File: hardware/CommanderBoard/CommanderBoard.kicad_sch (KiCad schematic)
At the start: 42 parts, among them J1 Conn_01x22, J1BUS1 Conn_02x04_Odd_Even, J1BUS2 Conn_02x04_Odd_Even, J2 Conn_01x22, J2BUS1 Conn_01x02, J2BUS2 Conn_01x02, J3 HUB75, J4 Conn_01x22, SW1 SW_SPDT, SW2 SW_DP3T, SW3 SW_DP3T, SW4 SW_DP3T

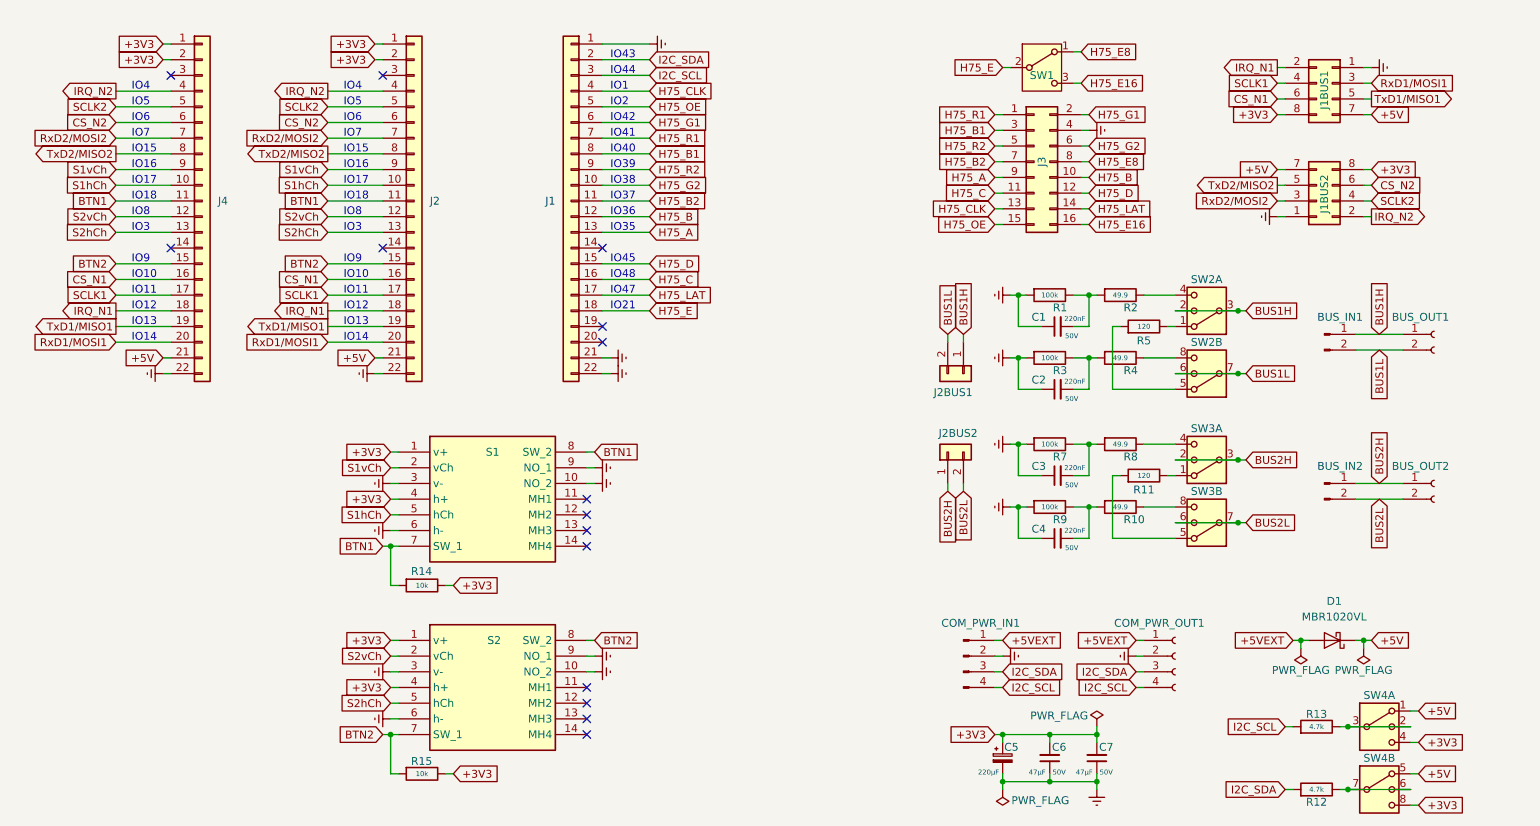
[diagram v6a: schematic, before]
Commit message: Minor imrpovements in positions and footprints.
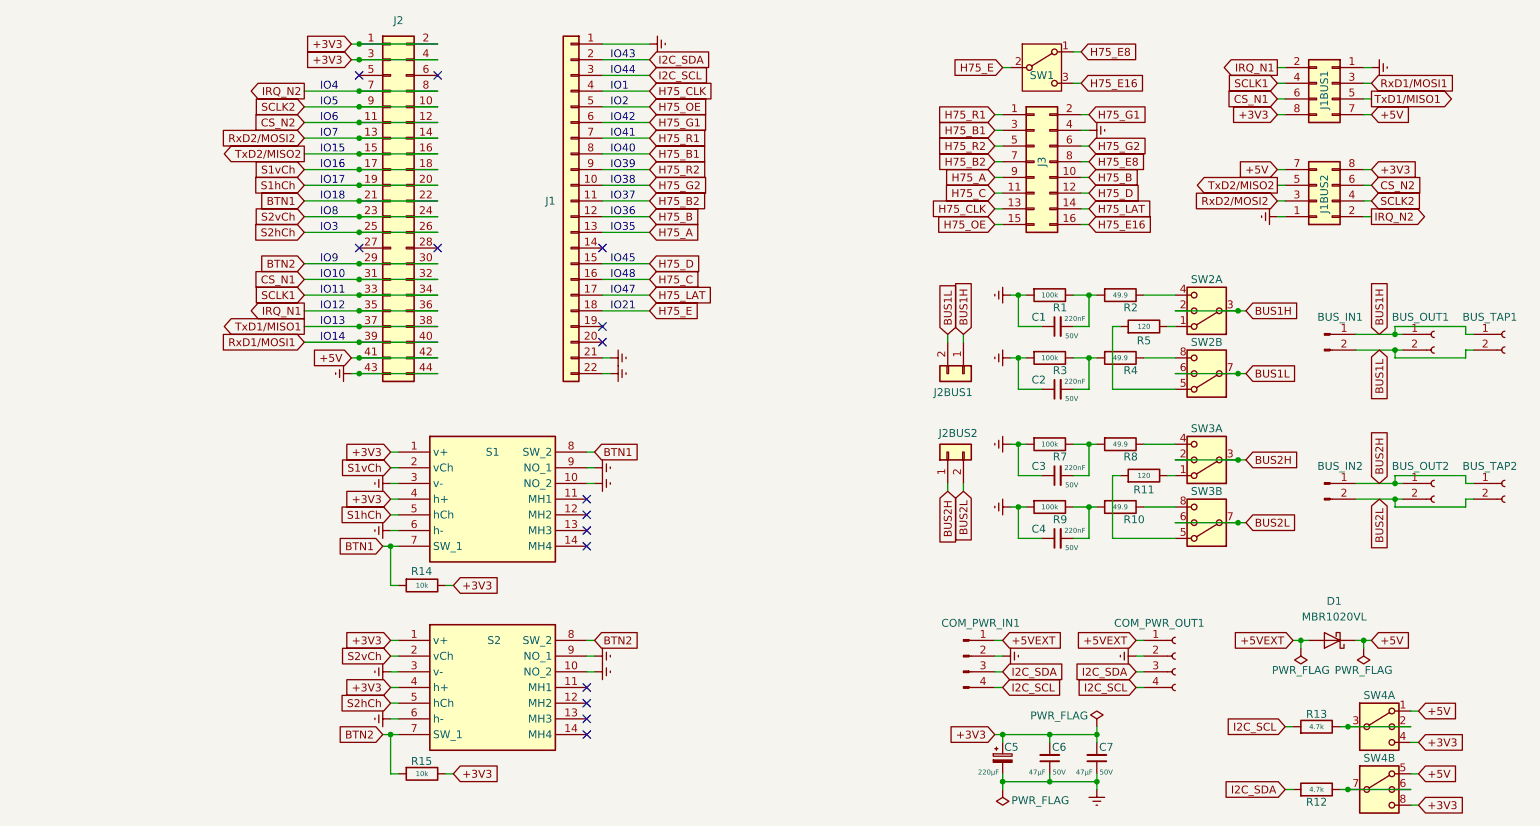
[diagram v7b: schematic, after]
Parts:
- removed J4: Conn_01x22, Connector_PinSocket_2.54mm:PinSocket_1x22_P2.54mm_Vertical, symbol Connector_Generic:Conn_01x22
- added BUS_TAP1, BUS_TAP2: Conn_01x02_Socket, Connector_PinHeader_2.54mm:PinHeader_1x02_P2.54mm_Vertical, symbol Connector:Conn_01x02_Socket
- C5: footprint Capacitor_SMD:CP_Elec_6.3x7.7 -> Capacitor_THT:CP_Radial_D6.3mm_P2.50mm
- J2: value Conn_01x22 -> Conn_02x22; footprint Connector_PinSocket_2.54mm:PinSocket_1x22_P2.54mm_Vertical -> Connector_PinSocket_2.54mm:PinSocket_2x22_P2.54mm_Vertical; symbol Connector_Generic:Conn_01x22 -> Connector_Generic:Conn_02x22_Odd_Even
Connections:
- net +3V3: now also J2.3 (Pin_3), J2.4 (Pin_4)
- net +5V: now also J2.41 (Pin_41), J2.42 (Pin_42); no longer J2.21 (Pin_21)
- net BTN1: now also J2.21 (Pin_21), J2.22 (Pin_22); no longer J2.11 (Pin_11)
- net BTN2: now also J2.29 (Pin_29), J2.30 (Pin_30); no longer J2.15 (Pin_15)
- net BUS1H: now also BUS_TAP1.1 (Pin_1)
- net BUS1L: now also BUS_TAP1.2 (Pin_2)
- net BUS2H: now also BUS_TAP2.1 (Pin_1)
- net BUS2L: now also BUS_TAP2.2 (Pin_2)
- net CS_N1: now also J2.31 (Pin_31), J2.32 (Pin_32); no longer J2.16 (Pin_16)
- net CS_N2: now also J2.11 (Pin_11), J2.12 (Pin_12); no longer J2.6 (Pin_6)
- net GNDREF: now also J2.43 (Pin_43), J2.44 (Pin_44); no longer J2.22 (Pin_22)
- net IRQ_N1: now also J2.35 (Pin_35), J2.36 (Pin_36); no longer J2.18 (Pin_18)
- net IRQ_N2: now also J2.7 (Pin_7), J2.8 (Pin_8); no longer J2.4 (Pin_4)
- net RxD1/MOSI1: now also J2.39 (Pin_39), J2.40 (Pin_40); no longer J2.20 (Pin_20)
- net RxD2/MOSI2: now also J2.13 (Pin_13), J2.14 (Pin_14); no longer J2.7 (Pin_7)
- net S1hCh: now also J2.19 (Pin_19), J2.20 (Pin_20); no longer J2.10 (Pin_10)
- net S1vCh: now also J2.17 (Pin_17), J2.18 (Pin_18); no longer J2.9 (Pin_9)
- net S2hCh: now also J2.25 (Pin_25), J2.26 (Pin_26); no longer J2.13 (Pin_13)
- net S2vCh: now also J2.23 (Pin_23), J2.24 (Pin_24); no longer J2.12 (Pin_12)
- net SCLK1: now also J2.33 (Pin_33), J2.34 (Pin_34); no longer J2.17 (Pin_17)
- net SCLK2: now also J2.10 (Pin_10), J2.9 (Pin_9); no longer J2.5 (Pin_5)
- net TxD1/MISO1: now also J2.37 (Pin_37), J2.38 (Pin_38); no longer J2.19 (Pin_19)
- net TxD2/MISO2: now also J2.15 (Pin_15), J2.16 (Pin_16); no longer J2.8 (Pin_8)
